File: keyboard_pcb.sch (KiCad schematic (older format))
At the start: 5 parts, among them J1 USB, J2 , J3 Power, J4 I2C, U1 Teensy4.0

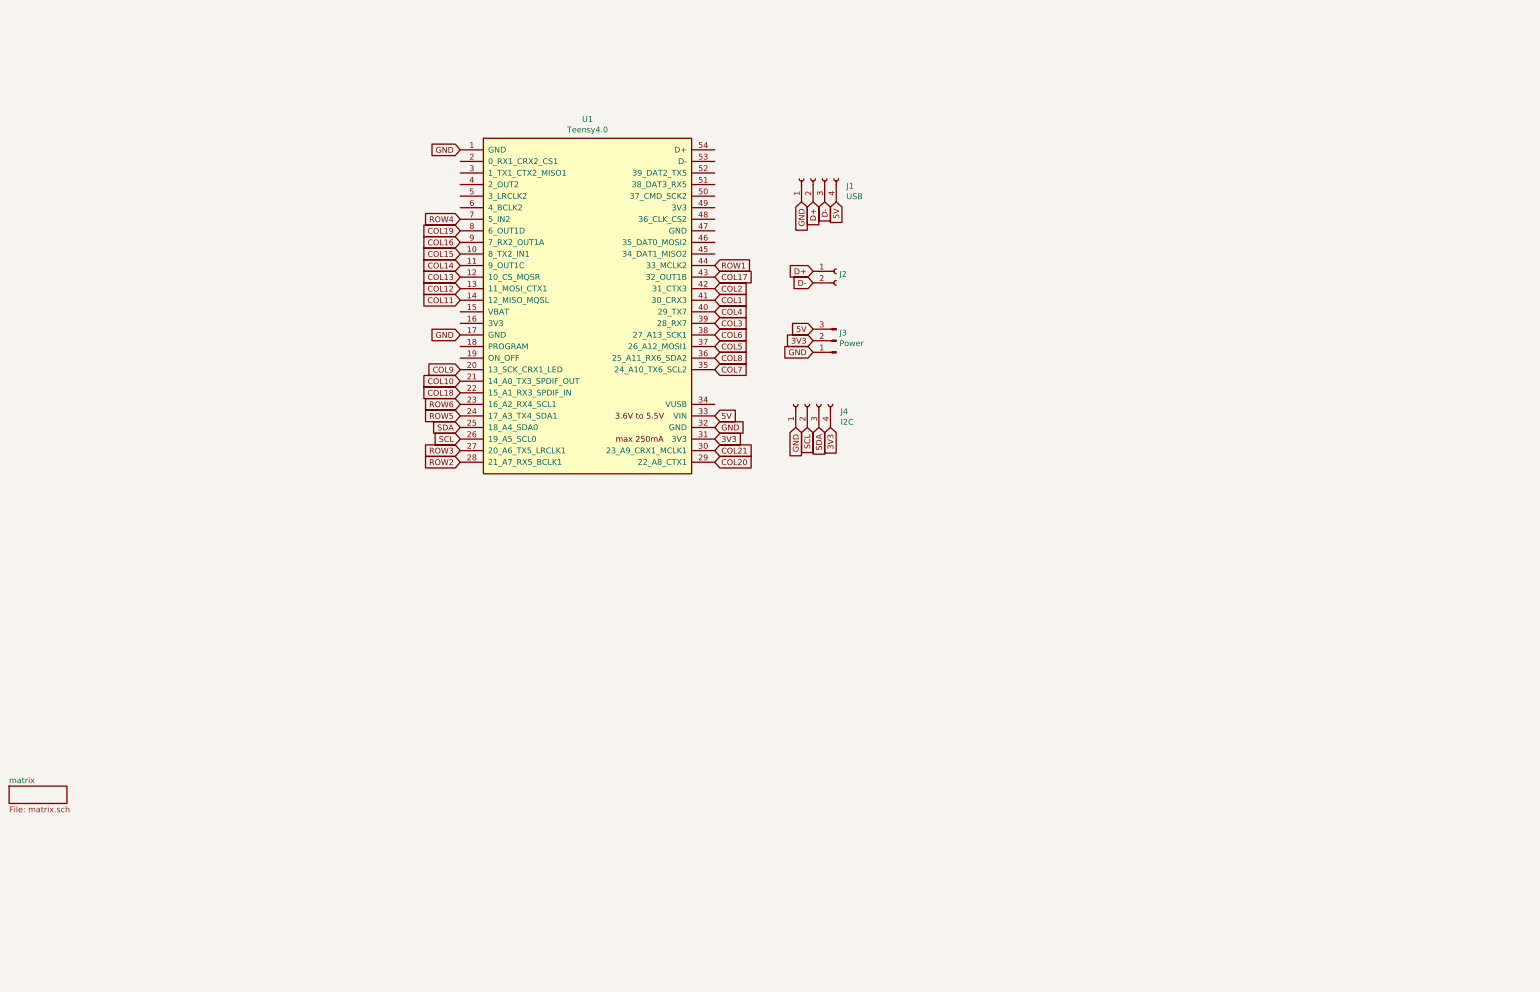
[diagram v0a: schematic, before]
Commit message: Put schematic onto one page
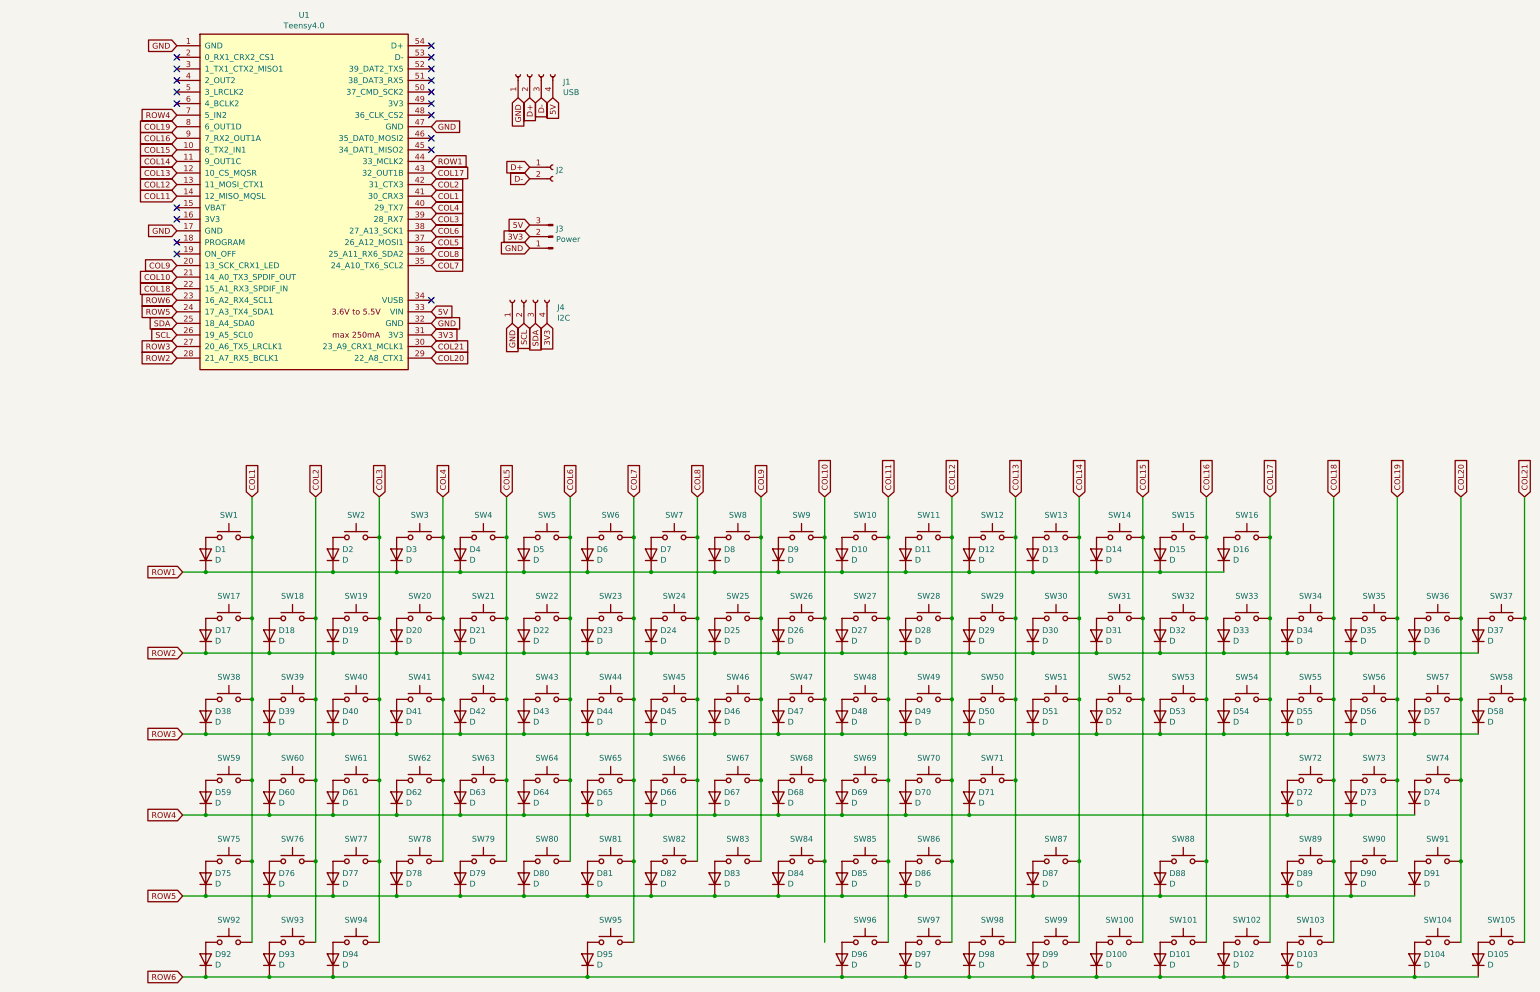
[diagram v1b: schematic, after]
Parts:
- added D1, D10, D100, D101, D102, D103, D104, D105, D11, D12, D13, D14, D15, D16, D17, D18, D19, D2, D20, D21, D22, D23, D24, D25, D26, D27, D28, D29, D3, D30, D31, D32, D33, D34, D35, D36, D37, D38, D39, D4, D40, D41, D42, D43, D44, D45, D46, D47, D48, D49, D5, D50, D51, D52, D53, D54, D55, D56, D57, D58, D59, D6, D60, D61, D62, D63, D64, D65, D66, D67, D68, D69, D7, D70, D71, D72, D73, D74, D75, D76, D77, D78, D79, D8, D80, D81, D82, D83, D84, D85, D86, D87, D88, D89, D9, D90, D91, D92, D93, D94, D95, D96, D97, D98, D99: D, Diode_THT:D_DO-35_SOD27_P7.62mm_Horizontal, symbol Device:D
- added SW1, SW10, SW100, SW101, SW102, SW104, SW11, SW12, SW13, SW14, SW15, SW16, SW17, SW18, SW19, SW2, SW20, SW21, SW22, SW23, SW24, SW25, SW26, SW27, SW28, SW29, SW3, SW31, SW32, SW33, SW34, SW35, SW36, SW37, SW39, SW4, SW40, SW41, SW42, SW43, SW44, SW45, SW46, SW47, SW48, SW49, SW5, SW50, SW52, SW53, SW54, SW55, SW56, SW57, SW6, SW60, SW61, SW62, SW63, SW64, SW65, SW66, SW67, SW68, SW69, SW7, SW70, SW71, SW72, SW73, SW74, SW76, SW77, SW78, SW79, SW8, SW80, SW81, SW82, SW83, SW84, SW85, SW86, SW88, SW89, SW9, SW90, SW91: SW_Push, Button_Switch_Keyboard:SW_Cherry_MX_1.00u_PCB, symbol Switch:SW_Push
- added SW103, SW30: SW_Push, Button_Switch_Keyboard:SW_Cherry_MX_2.00u_PCB, symbol Switch:SW_Push
- added SW105, SW58: SW_Push, Button_Switch_Keyboard:SW_Cherry_MX_2.00u_Vertical_PCB, symbol Switch:SW_Push
- added SW38: SW_Push, Button_Switch_Keyboard:SW_Cherry_MX_1.50u_PCB, symbol Switch:SW_Push
- added SW51: SW_Push, Button_Switch_Keyboard:SW_Cherry_MX_ISOEnter_PCB, symbol Switch:SW_Push
- added SW59: SW_Push, Button_Switch_Keyboard:SW_Cherry_MX_1.75u_PCB, symbol Switch:SW_Push
- added SW75, SW92, SW93, SW94, SW96, SW97, SW98, SW99: SW_Push, Button_Switch_Keyboard:SW_Cherry_MX_1.25u_PCB, symbol Switch:SW_Push
- added SW87: SW_Push, Button_Switch_Keyboard:SW_Cherry_MX_2.75u_PCB, symbol Switch:SW_Push
- added SW95: SW_Push, Button_Switch_Keyboard:SW_Cherry_MX_6.25u_PCB, symbol Switch:SW_Push
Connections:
- net COL1: now also SW1.2, SW17.2, SW38.2, SW59.2, SW75.2, SW92.2
- net COL10: now also SW26.2, SW47.2, SW68.2, SW84.2, SW9.2
- net COL11: now also SW10.2, SW27.2, SW48.2, SW69.2, SW85.2, SW96.2
- net COL12: now also SW11.2, SW28.2, SW49.2, SW70.2, SW86.2, SW97.2
- net COL13: now also SW12.2, SW29.2, SW50.2, SW71.2, SW98.2
- net COL14: now also SW13.2, SW30.2, SW51.2, SW87.2, SW99.2
- net COL15: now also SW100.2, SW14.2, SW31.2, SW52.2
- net COL16: now also SW101.2, SW15.2, SW32.2, SW53.2, SW88.2
- net COL17: now also SW102.2, SW16.2, SW33.2, SW54.2
- net COL18: now also SW103.2, SW34.2, SW55.2, SW72.2, SW89.2
- net COL19: now also SW35.2, SW56.2, SW73.2, SW90.2
- net COL2: now also SW18.2, SW39.2, SW60.2, SW76.2, SW93.2
- net COL20: now also SW104.2, SW36.2, SW57.2, SW74.2, SW91.2
- net COL21: now also SW105.2, SW37.2, SW58.2
- net COL3: now also SW19.2, SW2.2, SW40.2, SW61.2, SW77.2, SW94.2
- net COL4: now also SW20.2, SW3.2, SW41.2, SW62.2, SW78.2
- net COL5: now also SW21.2, SW4.2, SW42.2, SW63.2, SW79.2
- net COL6: now also SW22.2, SW43.2, SW5.2, SW64.2, SW80.2
- net COL7: now also SW23.2, SW44.2, SW6.2, SW65.2, SW81.2, SW95.2
- net COL8: now also SW24.2, SW45.2, SW66.2, SW7.2, SW82.2
- net COL9: now also SW25.2, SW46.2, SW67.2, SW8.2, SW83.2
- net GND: now also U1.47 (GND)
- net ROW1: now also D1.1 (K), D10.1 (K), D11.1 (K), D12.1 (K), D13.1 (K), D14.1 (K), D15.1 (K), D16.1 (K), D2.1 (K), D3.1 (K), D4.1 (K), D5.1 (K), D6.1 (K), D7.1 (K), D8.1 (K), D9.1 (K)
- net ROW2: now also D17.1 (K), D18.1 (K), D19.1 (K), D20.1 (K), D21.1 (K), D22.1 (K), D23.1 (K), D24.1 (K), D25.1 (K), D26.1 (K), D27.1 (K), D28.1 (K), D29.1 (K), D30.1 (K), D31.1 (K), D32.1 (K), D33.1 (K), D34.1 (K), D35.1 (K), D36.1 (K), D37.1 (K)
- net ROW3: now also D38.1 (K), D39.1 (K), D40.1 (K), D41.1 (K), D42.1 (K), D43.1 (K), D44.1 (K), D45.1 (K), D46.1 (K), D47.1 (K), D48.1 (K), D49.1 (K), D50.1 (K), D51.1 (K), D52.1 (K), D53.1 (K), D54.1 (K), D55.1 (K), D56.1 (K), D57.1 (K), D58.1 (K)
- net ROW4: now also D59.1 (K), D60.1 (K), D61.1 (K), D62.1 (K), D63.1 (K), D64.1 (K), D65.1 (K), D66.1 (K), D67.1 (K), D68.1 (K), D69.1 (K), D70.1 (K), D71.1 (K), D72.1 (K), D73.1 (K), D74.1 (K)
- net ROW5: now also D75.1 (K), D76.1 (K), D77.1 (K), D78.1 (K), D79.1 (K), D80.1 (K), D81.1 (K), D82.1 (K), D83.1 (K), D84.1 (K), D85.1 (K), D86.1 (K), D87.1 (K), D88.1 (K), D89.1 (K), D90.1 (K), D91.1 (K)
- net ROW6: now also D100.1 (K), D101.1 (K), D102.1 (K), D103.1 (K), D104.1 (K), D105.1 (K), D92.1 (K), D93.1 (K), D94.1 (K), D95.1 (K), D96.1 (K), D97.1 (K), D98.1 (K), D99.1 (K)
- new net: D1.2 (A), SW1.1
- new net: D2.2 (A), SW2.1
- new net: D3.2 (A), SW3.1
- new net: D4.2 (A), SW4.1
- new net: D5.2 (A), SW5.1
- new net: D6.2 (A), SW6.1
- new net: D7.2 (A), SW7.1
- new net: D8.2 (A), SW8.1
- new net: D9.2 (A), SW9.1
- new net: D10.2 (A), SW10.1
- new net: D11.2 (A), SW11.1
- new net: D12.2 (A), SW12.1
- new net: D13.2 (A), SW13.1
- new net: D14.2 (A), SW14.1
- new net: D15.2 (A), SW15.1
- new net: D16.2 (A), SW16.1
- new net: D17.2 (A), SW17.1
- new net: D18.2 (A), SW18.1
- new net: D19.2 (A), SW19.1
- new net: D20.2 (A), SW20.1
- new net: D21.2 (A), SW21.1
- new net: D22.2 (A), SW22.1
- new net: D23.2 (A), SW23.1
- new net: D24.2 (A), SW24.1
- new net: D25.2 (A), SW25.1
- new net: D26.2 (A), SW26.1
- new net: D27.2 (A), SW27.1
- new net: D28.2 (A), SW28.1
- new net: D29.2 (A), SW29.1
- new net: D30.2 (A), SW30.1
- new net: D31.2 (A), SW31.1
- new net: D32.2 (A), SW32.1
- new net: D33.2 (A), SW33.1
- new net: D34.2 (A), SW34.1
- new net: D35.2 (A), SW35.1
- new net: D36.2 (A), SW36.1
- new net: D37.2 (A), SW37.1
- new net: D38.2 (A), SW38.1
- new net: D39.2 (A), SW39.1
- new net: D40.2 (A), SW40.1
- new net: D41.2 (A), SW41.1
- new net: D42.2 (A), SW42.1
- new net: D43.2 (A), SW43.1
- new net: D44.2 (A), SW44.1
- new net: D45.2 (A), SW45.1
- new net: D46.2 (A), SW46.1
- new net: D47.2 (A), SW47.1
- new net: D48.2 (A), SW48.1
- new net: D49.2 (A), SW49.1
- new net: D50.2 (A), SW50.1
- new net: D55.2 (A), SW55.1
- new net: D56.2 (A), SW56.1
- new net: D57.2 (A), SW57.1
- new net: D59.2 (A), SW59.1
- new net: D60.2 (A), SW60.1
- new net: D61.2 (A), SW61.1
- new net: D62.2 (A), SW62.1
- new net: D63.2 (A), SW63.1
- new net: D64.2 (A), SW64.1
- new net: D65.2 (A), SW65.1
- new net: D66.2 (A), SW66.1
- new net: D67.2 (A), SW67.1
- new net: D68.2 (A), SW68.1
- new net: D69.2 (A), SW69.1
- new net: D70.2 (A), SW70.1
- new net: D71.2 (A), SW71.1
- new net: D72.2 (A), SW72.1
- new net: D73.2 (A), SW73.1
- new net: D74.2 (A), SW74.1
- new net: D51.2 (A), SW51.1
- new net: D52.2 (A), SW52.1
- new net: D53.2 (A), SW53.1
- new net: D54.2 (A), SW54.1
- new net: D58.2 (A), SW58.1
- new net: D75.2 (A), SW75.1
- new net: D76.2 (A), SW76.1
- new net: D77.2 (A), SW77.1
- new net: D78.2 (A), SW78.1
- new net: D79.2 (A), SW79.1
- new net: D80.2 (A), SW80.1
- new net: D81.2 (A), SW81.1
- new net: D82.2 (A), SW82.1
- new net: D83.2 (A), SW83.1
- new net: D84.2 (A), SW84.1
- new net: D85.2 (A), SW85.1
- new net: D86.2 (A), SW86.1
- new net: D89.2 (A), SW89.1
- new net: D90.2 (A), SW90.1
- new net: D91.2 (A), SW91.1
- new net: D87.2 (A), SW87.1
- new net: D88.2 (A), SW88.1
- new net: D92.2 (A), SW92.1
- new net: D93.2 (A), SW93.1
- new net: D94.2 (A), SW94.1
- new net: D95.2 (A), SW95.1
- new net: D96.2 (A), SW96.1
- new net: D97.2 (A), SW97.1
- new net: D98.2 (A), SW98.1
- new net: D99.2 (A), SW99.1
- new net: D100.2 (A), SW100.1
- new net: D101.2 (A), SW101.1
- new net: D102.2 (A), SW102.1
- new net: D103.2 (A), SW103.1
- new net: D104.2 (A), SW104.1
- new net: D105.2 (A), SW105.1
- no-connect marks 0 -> 19
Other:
- moved on the sheet: J1, J2, J3, J4, U1
